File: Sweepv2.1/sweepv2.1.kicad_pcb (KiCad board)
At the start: 2 copper layers, 216.9 x 86.9 mm, 51 parts, among them J1 AudioJack4dpb, J2 AudioJack4dpb, SW10 SW_Push, SW11 SW_Push, SW11_r1 SW_Push, SW12 SW_Push, SW12_r1 SW_Push, SW13_r1 SW_Push, SW14 SW_Push, SW15 SW_Push, SW15_r1 SW_Push, SW16 SW_Push, SW16_r1 SW_Push, SW17 SW_Push, SW17_r1 SW_Push, SW18 SW_Push, SW18_r1 SW_Push, SW2 SW_Push, SW20 SW_Push, SW20_r1 SW_Push, SW21 SW_Push, SW21_r1 SW_Push, SW2_r1 SW_Push, SW3 SW_Push, SW3_r1 SW_Push, SW4 SW_Push, SW4_r1 SW_Push, SW5 SW_Push, SW5_r1 SW_Push, SW6 SW_Push, SW6_r1 SW_Push, SW7_r1 SW_Push, SW8 SW_Push, SW8_r1 SW_Push, SW9 SW_Push, SW9_r1 SW_Push, U1 ProMicro-kbd, U2 ProMicro-kbd

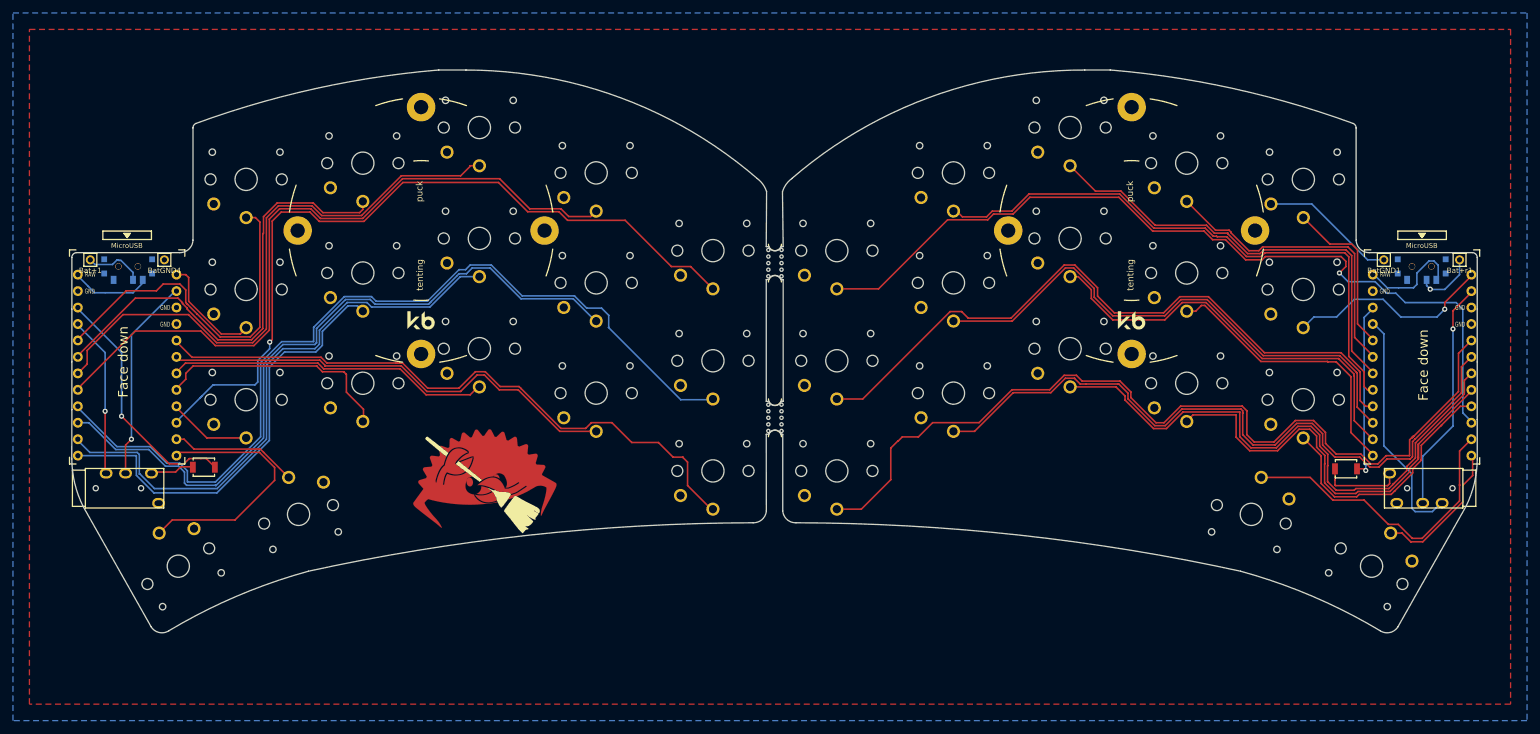
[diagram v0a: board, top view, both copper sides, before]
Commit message: Added holes for JST connector
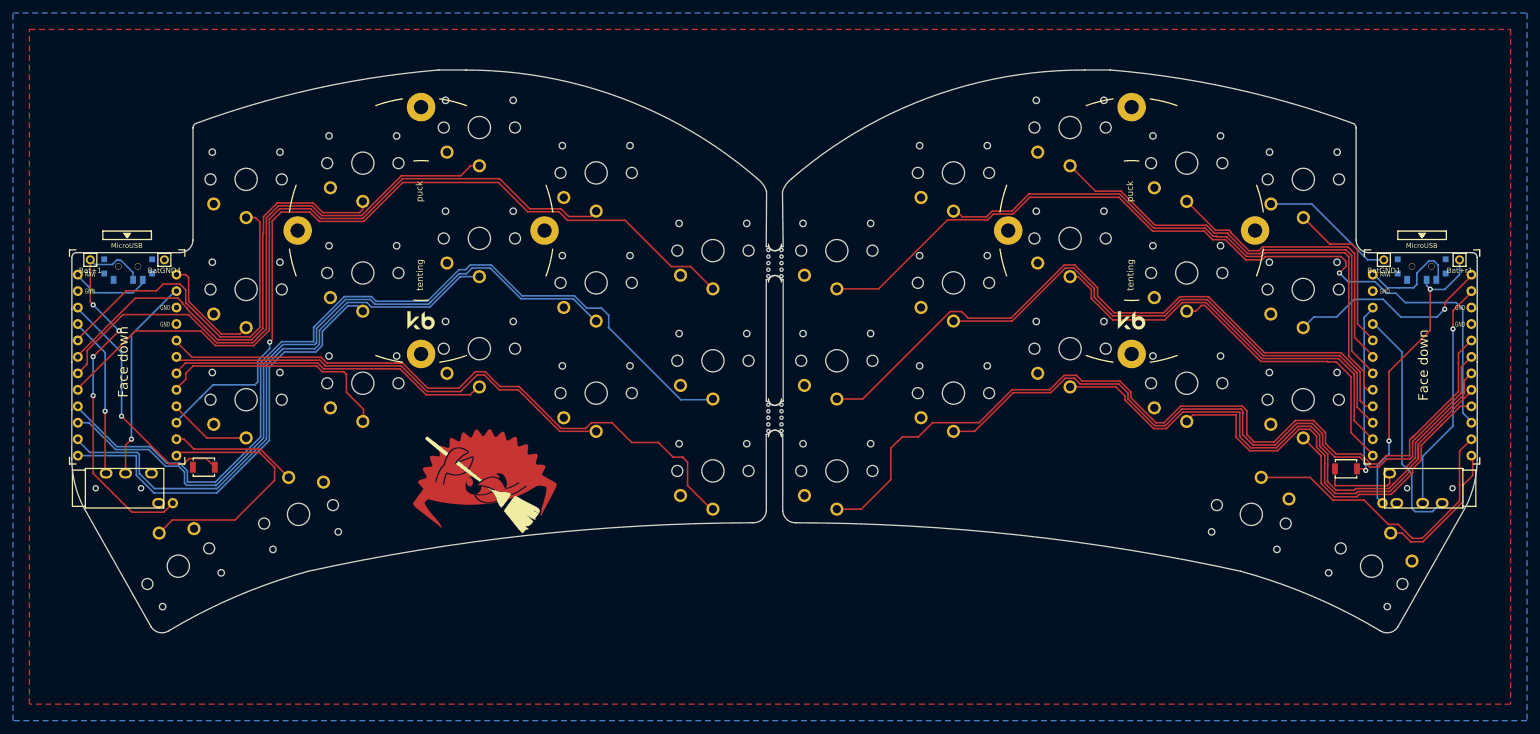
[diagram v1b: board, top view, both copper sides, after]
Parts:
- added ?: , , F.Cu at (38.1, 87.8)
- added ?: , , F.Cu at (224.1, 88.8)
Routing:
- net BT+: track 9.11 -> 60.9 mm, vias 0 -> 4
- net BT+_r: track 9.45 -> 46.2 mm, vias 1 -> 2
- net gnd: track 40.7 -> 34.1 mm
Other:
- net class Default removed
